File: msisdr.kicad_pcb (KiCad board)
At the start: 2 copper layers, 46.3 x 90.7 mm, 80 parts, among them J1 VCC_GPIO, J10 SMA_VHF1, J11 USB_OTG, J2 GPIO0, J3 GPIO1, J4 GPIO2, J5 GPIO3, J6 SMA_0_30MHZ, J7 SMA_30_60MHZ, J8 SMA_VHF2, J9 SMA_UHF, U1 msi2500, U2 msi001, U3 RT9193-28, U4 XC6206P302MR, Y1 24MHz, Y2 24MHZ

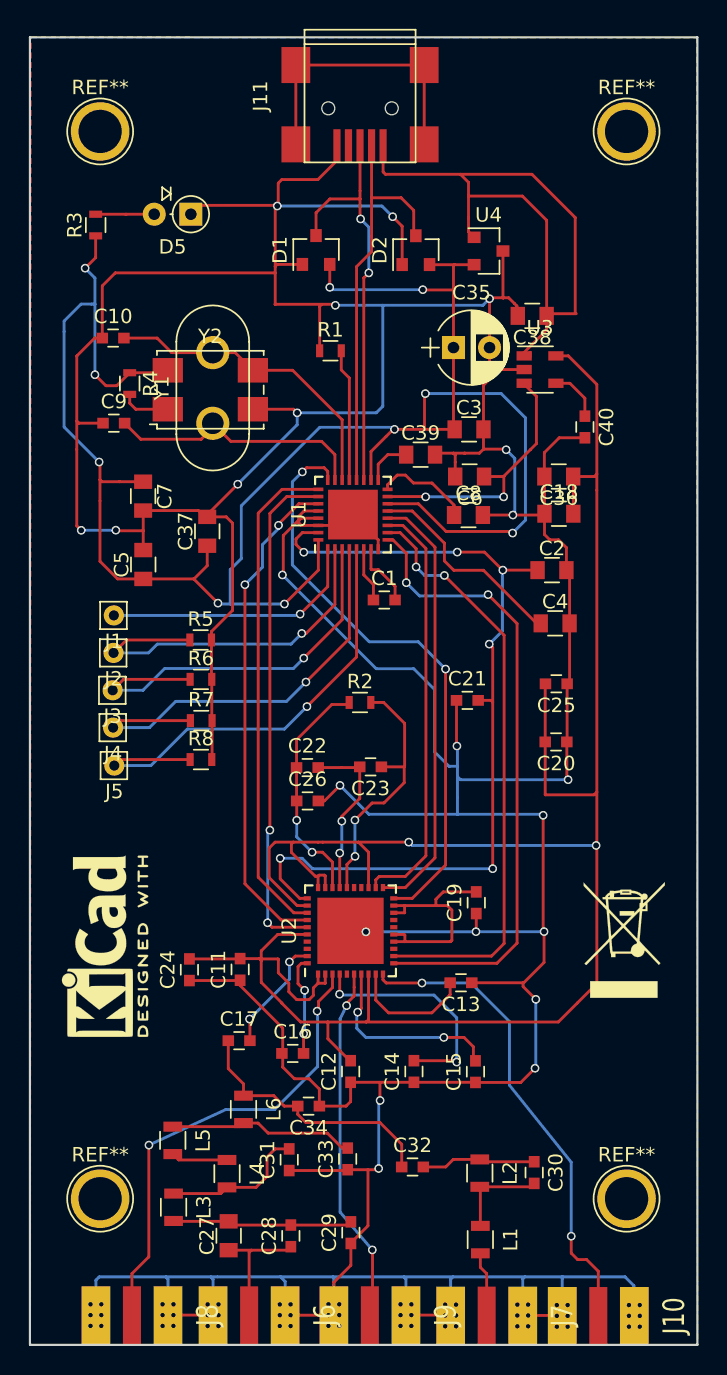
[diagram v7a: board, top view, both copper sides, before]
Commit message: fix bugs 1. not connect msi001 4 vcc to VRF 2. msi2500 VCC_GPIO connect to 1uF to GND 3. REF_CLK should use 10nF connect
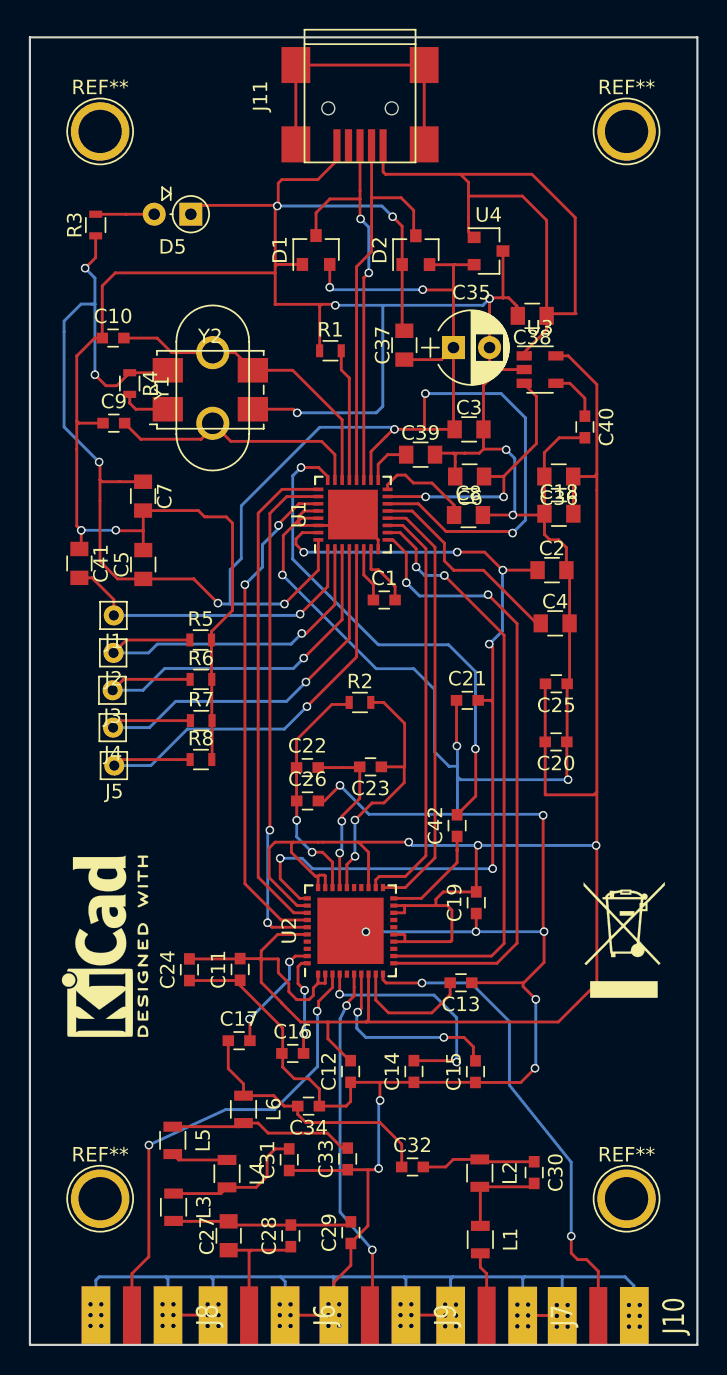
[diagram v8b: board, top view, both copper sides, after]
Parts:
- added C41: 1UF, Capacitors_SMD:C_0805, F.Cu at (116.6, 80.0)
- added C42: 10nF, Capacitors_SMD:C_0603, F.Cu at (142.8, 98.1)
- C23: value 6800pF -> 33nF
- U4: value XC6206P302MR -> AP7313-30SAG
- moved C37 18.8 mm to (139.1, 64.8)
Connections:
- C19 pad 2: Net-(C19-Pad2) -> VRF
- U1 pad 24: REFCLK -> Net-(C42-Pad2)
- U2 pad 14: Net-(C19-Pad2) -> VRF
- U2 pad 15: Net-(C19-Pad2) -> VRF
- U2 pad 18: Net-(C19-Pad2) -> VRF
- U2 pad 19: Net-(C19-Pad2) -> VRF
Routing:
- net Net-(C42-Pad2): track 0.00 -> 35.3 mm, vias 0 -> 2
- net REFCLK: track 41.1 -> 7.36 mm, vias 2 -> 0
- net VRF: track 150.1 -> 169.8 mm, vias 2 -> 3
- net Net-(C19-Pad2): track 16.3 -> 0.00 mm
- net Net-(C41-Pad2): track 18.2 -> 22.4 mm
- net GND: track 469.5 -> 465.7 mm, vias 22 -> 21
- net VDIG: track 142.8 -> 143.9 mm
- removed copper zone on B.Cu, net GND
- removed copper zone on F.Cu, net GND
